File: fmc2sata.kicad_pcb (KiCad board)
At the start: 2 copper layers, 51 x 61 mm, 32 parts, among them J1 ASP-134488-01, J2 1-2199230-6, J3 10034814-001LF, U1 TPS565208, U2 TPS565208

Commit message: Cleanup
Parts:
- removed C1, C2, C6, C7: C_10u_25V_0603, antmicro-footprints:0603-cap
- removed C10, C4, C5, C9: C_22u_0805_10V, antmicro-footprints:0805-cap
- removed C11, C12, C13, C14: C_10n_0402, antmicro-footprints:0402-cap
- removed C3, C8: C_100n_0603, antmicro-footprints:0603-cap
- removed D1: KP-1608CGCK, antmicro-footprints:LED_0603
- removed L1: WE_74437336022, antmicro-footprints:WE_74437336022
- removed L2: WE_74437336033, antmicro-footprints:WE_74437336033
- removed R1: R_33k2_0402, antmicro-footprints:0402-res
- removed R2, R5, R8: R_10k_0402, antmicro-footprints:0402-res
- removed R3, R7, R9: R_0R_0402, antmicro-footprints:0402-res
- removed R4: R_54k9_0402, antmicro-footprints:0402-res
- removed R6: R_330R_0402, antmicro-footprints:0402-res
- removed U1, U2: TPS565208, antmicro-footprints:SOT-23-6
- J3: moved to B.Cu
- turned J3 to 270 degrees
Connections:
- net Net-(J3-Pad2A) renamed /EXT_SATA_A_P
- net Net-(J3-Pad3A) renamed /EXT_SATA_A_N
- net Net-(J3-Pad5A) renamed /EXT_SATA_B_N
- net Net-(J3-Pad6A) renamed /EXT_SATA_B_P
- J2 pad 41: Net-(C14-Pad2) -> /M2_SATA_B_P
- J2 pad 43: Net-(C12-Pad2) -> /M2_SATA_B_N
- J2 pad 47: Net-(C13-Pad2) -> /M2_SATA_A_N
- J2 pad 49: Net-(C11-Pad2) -> /M2_SATA_A_P
- J3 pad 13B: Net-(J3-Pad13B) -> +12V
- J3 pad 14B: Net-(J3-Pad13B) -> +12V
- J3 pad 15B: Net-(J3-Pad13B) -> +12V
- J3 pad 1B: Net-(J3-Pad1B) -> +3V3
- J3 pad 2B: Net-(J3-Pad1B) -> +3V3
- J3 pad 3B: Net-(J3-Pad1B) -> +3V3
- J3 pad 7B: Net-(J3-Pad7B) -> +5V
- J3 pad 8B: Net-(J3-Pad7B) -> +5V
- J3 pad 9B: Net-(J3-Pad7B) -> +5V
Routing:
- net GND: track 0.00 -> 1.86 mm, vias 0 -> 2
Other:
- copper layers 2 -> 4
- net class Default: trace_width 0.25 -> 0.15; via_dia 0.8 -> 0.55; via_drill 0.4 -> 0.15
- net class Z100 added: clearance 0.2, trace_width 0.15, via_dia 0.55, via_drill 0.15
- rule trace_min: 0.2 -> 0.1
- rule via_min_drill: 0.3 -> 0.15
- rule via_min_size: 0.4 -> 0.55

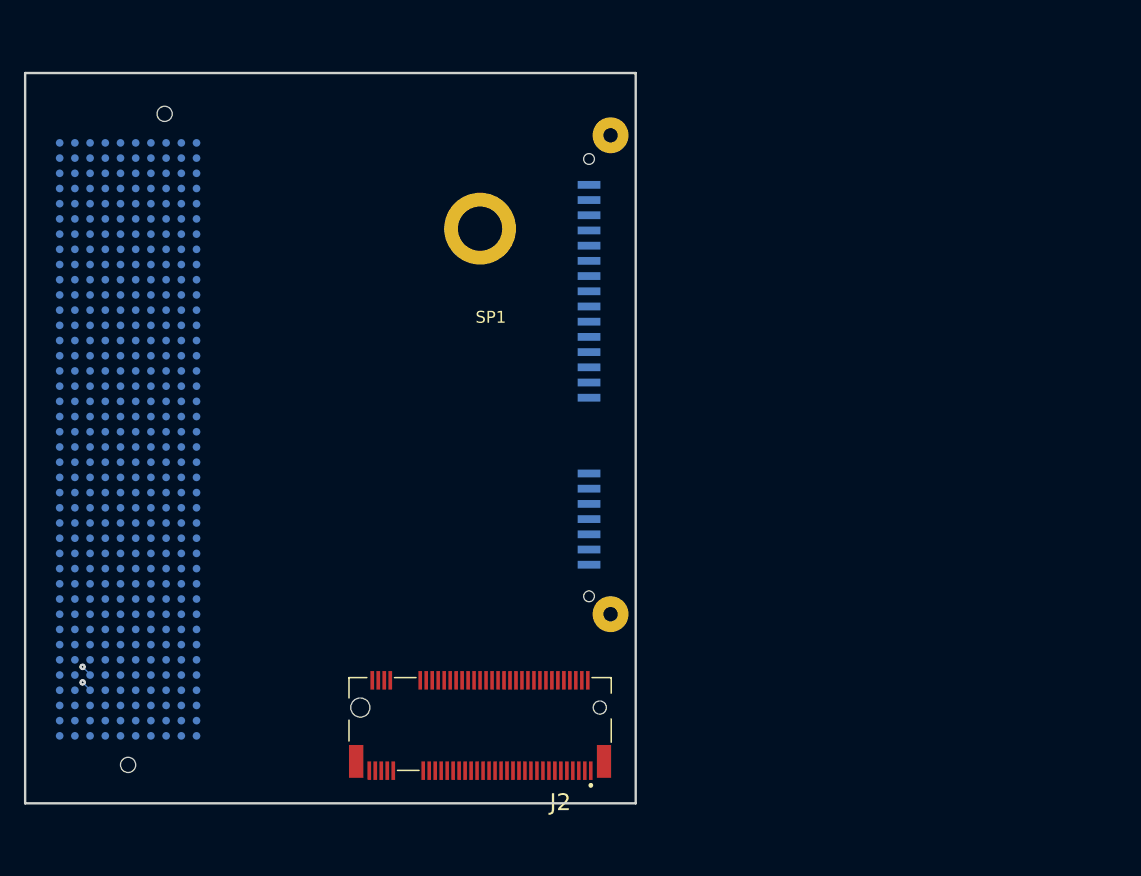
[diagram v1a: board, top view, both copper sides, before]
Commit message: Add initial component placement
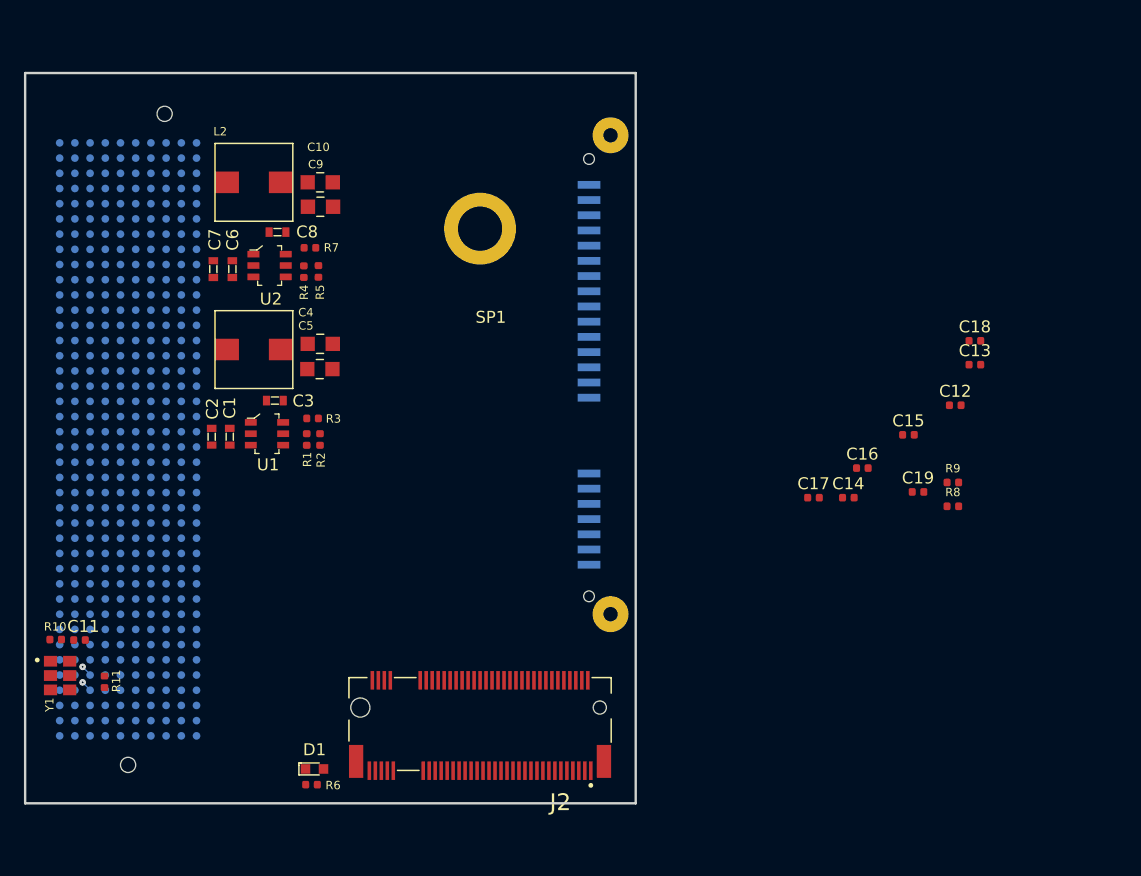
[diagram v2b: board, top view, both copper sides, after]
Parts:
- added C1: C_10u_25V_0603, antmicro-footprints:0603-cap, F.Cu at (89.1, 77.4)
- added C10: C_22u_0805_10V, antmicro-footprints:0805-cap, F.Cu at (96.7, 56.1)
- added C11: C_100n_0402, antmicro-footprints:0402-cap, F.Cu at (76.5, 94.4)
- added C12: C_10n_0402, antmicro-footprints:0402-cap, F.Cu at (149.7, 74.8)
- added C13: C_10n_0402, antmicro-footprints:0402-cap, F.Cu at (151.3, 71.4)
- added C14: C_10n_0402, antmicro-footprints:0402-cap, F.Cu at (140.8, 82.5)
- added C15: C_10n_0402, antmicro-footprints:0402-cap, F.Cu at (145.8, 77.2)
- added C16: C_10n_0402, antmicro-footprints:0402-cap, F.Cu at (141.9, 80.0)
- added C17: C_10n_0402, antmicro-footprints:0402-cap, F.Cu at (137.8, 82.5)
- added C18: C_10n_0402, antmicro-footprints:0402-cap, F.Cu at (151.3, 69.4)
- added C19: C_10n_0402, antmicro-footprints:0402-cap, F.Cu at (146.6, 82.0)
- added C2: C_10u_25V_0603, antmicro-footprints:0603-cap, F.Cu at (87.6, 77.4)
- added C3: C_100n_0603, antmicro-footprints:0603-cap, F.Cu at (92.9, 74.4)
- added C4: C_22u_0805_10V, antmicro-footprints:0805-cap, F.Cu at (96.7, 69.6)
- added C5: C_22u_0805_10V, antmicro-footprints:0805-cap, F.Cu at (96.6, 71.7)
- added C6: C_10u_25V_0603, antmicro-footprints:0603-cap, F.Cu at (89.3, 63.4)
- added C7: C_10u_25V_0603, antmicro-footprints:0603-cap, F.Cu at (87.7, 63.4)
- added C8: C_100n_0603, antmicro-footprints:0603-cap, F.Cu at (93.1, 60.3)
- added C9: C_22u_0805_10V, antmicro-footprints:0805-cap, F.Cu at (96.7, 58.2)
- added D1: KP-1608CGCK, antmicro-footprints:LED_0603, F.Cu at (96.2, 105.1)
- added L1: WE_74437336022, antmicro-footprints:WE_74437336022, F.Cu at (91.1, 70.1)
- added L2: WE_74438356220, antmicro-footprints:WE_74437336033, F.Cu at (91.1, 56.1)
- added R1: R_33k2_0402, antmicro-footprints:0402-res, F.Cu at (95.5, 77.6)
- added R10: R_1k_0402, antmicro-footprints:0402-res, F.Cu at (74.5, 94.3)
- added R11: R_100R_0402, antmicro-footprints:0402-res, F.Cu at (78.6, 97.8)
- added R2: R_10k_0402, antmicro-footprints:0402-res, F.Cu at (96.6, 77.6)
- added R3: R_0R_0402, antmicro-footprints:0402-res, F.Cu at (96.0, 75.8)
- added R4: R_54k9_0402, antmicro-footprints:0402-res, F.Cu at (95.3, 63.6)
- added R5: R_10k_0402, antmicro-footprints:0402-res, F.Cu at (96.5, 63.6)
- added R6: R_330R_0402, antmicro-footprints:0402-res, F.Cu at (95.9, 106.4)
- added R7: R_0R_0402, antmicro-footprints:0402-res, F.Cu at (95.8, 61.6)
- added R8: R_10k_0402, antmicro-footprints:0402-res, F.Cu at (149.5, 83.2)
- added R9: R_0R_0402, antmicro-footprints:0402-res, F.Cu at (149.5, 81.2)
- added U1: TPS565208, antmicro-footprints:SOT-23-6, F.Cu at (92.2, 77.1)
- added U2: TPS565208, antmicro-footprints:SOT-23-6, F.Cu at (92.4, 63.1)
- added Y1: AX3DAF1-150.0000, antmicro-footprints:AX3DAF1, F.Cu at (74.9, 97.3)

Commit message: Include FMC fastening holes
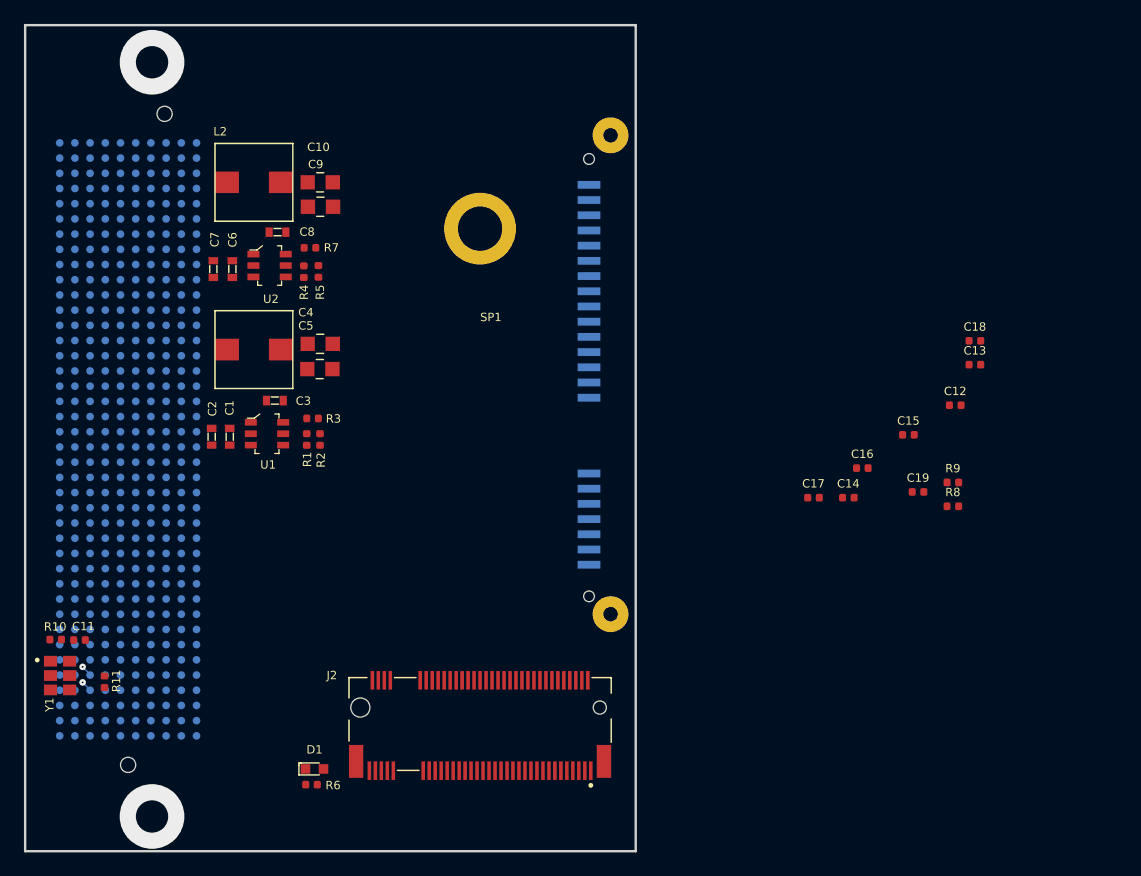
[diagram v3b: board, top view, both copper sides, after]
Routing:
- net (no net): vias 0 -> 2
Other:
- board size 51 x 61 mm -> 51 x 69 mm
